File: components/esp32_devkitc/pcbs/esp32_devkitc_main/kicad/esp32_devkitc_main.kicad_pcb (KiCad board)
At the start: 2 copper layers, 65 x 56 mm, 28 parts, among them J1 Conn_02x05_Odd_Even, J2 Conn_02x04_Odd_Even, J3 Conn_01x03_Male, J4 Conn_01x02, P1 Conn_02x20_Odd_Even, U1 ESP32-DEVKITC-32D

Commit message: small update
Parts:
- J4: moved to B.Cu
- P1: footprint Connector_PinSocket_2.54mm:PinSocket_2x20_P2.54mm_Vertical -> Connector_PinHeader_2.54mm:PinHeader_2x20_P2.54mm_Vertical; moved to F.Cu
- turned J4 to 90 degrees
- turned P1 to 90 degrees
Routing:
- net /SENS_5V_ANA: track 100.2 -> 100.9 mm

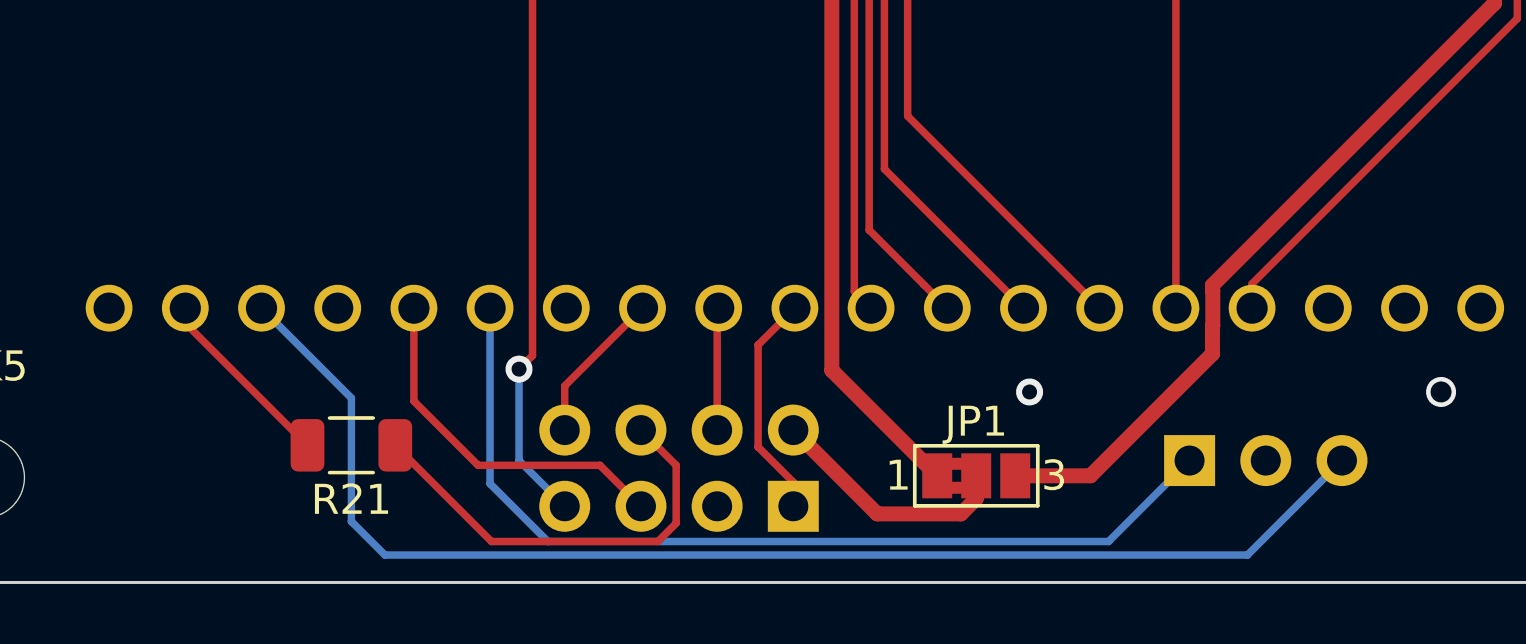
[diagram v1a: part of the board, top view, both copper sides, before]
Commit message: moves R21 below devkit
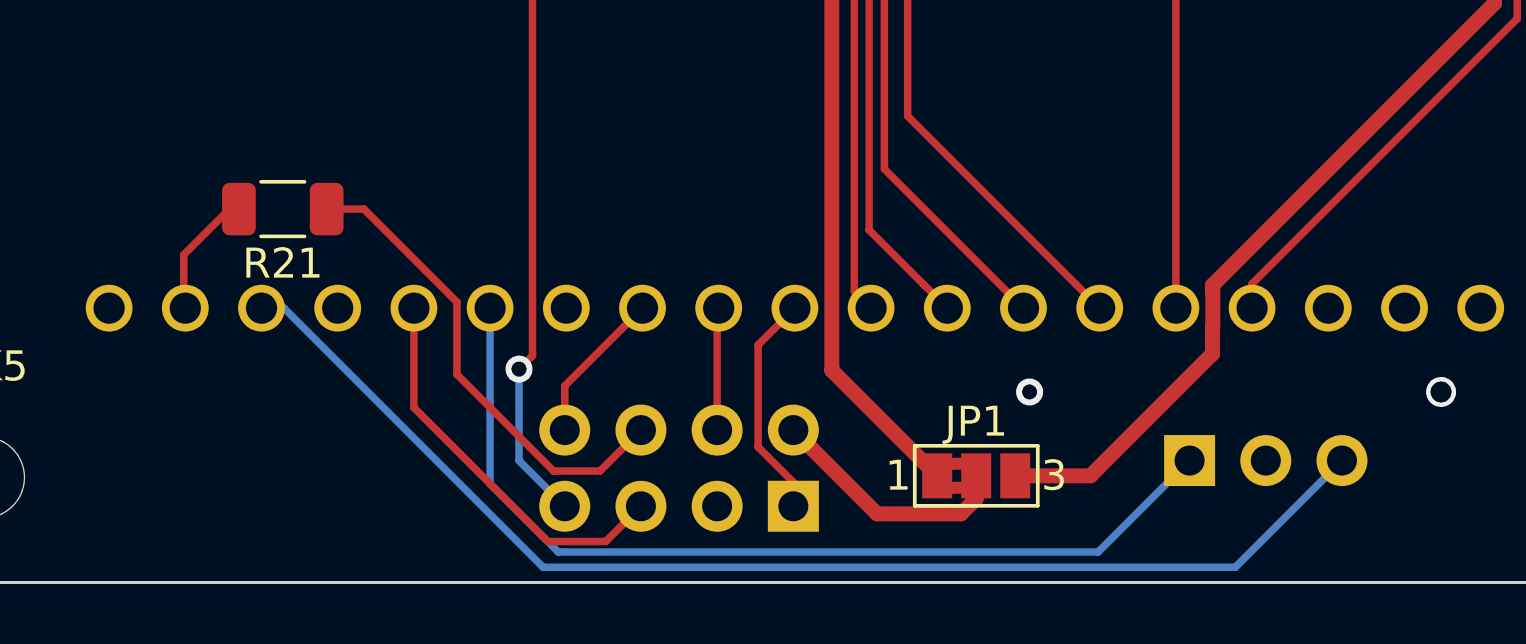
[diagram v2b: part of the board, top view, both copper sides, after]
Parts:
- moved R21 8.20 mm to (213.5, 137.6)
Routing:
- net /PROC_SCL: track 43.1 -> 41.1 mm
- net Net-(R21-Pad2): track 6.26 -> 4.27 mm
- net /DISP_MOSI: track 14.5 -> 16.1 mm
- net /DISP_CS_TOUCH: track 12.1 -> 13.2 mm
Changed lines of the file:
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@@
     (thickness 1.6)
     (drawings 21)
-    (tracks 261)
+    (tracks 263)
     (zones 0)
     (modules 28)
@@
     (pad_to_mask_clearance 0)
     (aux_axis_origin 200 150)
-    (grid_origin 200 150)
     (visible_elements 7FFFFFFF)
     (pcbplotparams
@@
   )
   (module Resistor_SMD:R_1206_3216Metric (layer F.Cu)
-    (at 215.748 145.428 180)
+    (at 213.462 137.554 180)
     (descr "Resistor SMD 1206 (3216 Metric), square (rectangular) end terminal, IPC_7351 nominal, (Body size source: IPC-SM-782 page 72, https://www.pcb-3d.com/wordpress/wp-content/uploads/ipc-sm-782a_amendment_1_and_2.pdf), generated with kicad-footprint-generator")
     (tags resistor)
@@
   (segment (start 246.7975 107.328) (end 244.45 107.328) (width 0.25) (layer F.Cu) (net 41))
   (via (at 244.45 107.328) (size 0.9) (drill 0.5) (layers F.Cu B.Cu) (net 41))
-  (segment (start 216.865011 149.085011) (end 245.618989 149.085011) (width 0.25) (layer B.Cu) (net 42))
-  (segment (start 215.748 147.968) (end 216.865011 149.085011) (width 0.25) (layer B.Cu) (net 42))
-  (segment (start 215.748 143.852) (end 215.748 147.968) (width 0.25) (layer B.Cu) (net 42))
-  (segment (start 245.618989 149.085011) (end 248.768 145.936) (width 0.25) (layer B.Cu) (net 42))
-  (segment (start 212.752 140.856) (end 215.748 143.852) (width 0.25) (layer B.Cu) (net 42))
-  (segment (start 220.372 146.711002) (end 222.295999 148.635001) (width 0.25) (layer B.Cu) (net 43))
-  (segment (start 240.988999 148.635001) (end 243.688 145.936) (width 0.25) (layer B.Cu) (net 43))
-  (segment (start 222.295999 148.635001) (end 240.988999 148.635001) (width 0.25) (layer B.Cu) (net 43))
+  (segment (start 245.212 149.492) (end 248.768 145.936) (width 0.25) (layer B.Cu) (net 42))
+  (segment (start 222.136 149.492) (end 245.212 149.492) (width 0.25) (layer B.Cu) (net 42))
+  (segment (start 213.5 140.856) (end 222.136 149.492) (width 0.25) (layer B.Cu) (net 42))
+  (segment (start 212.752 140.856) (end 213.5 140.856) (width 0.25) (layer B.Cu) (net 42))
+  (segment (start 240.64 148.984) (end 243.688 145.936) (width 0.25) (layer B.Cu) (net 43))
+  (segment (start 222.644998 148.984) (end 240.64 148.984) (width 0.25) (layer B.Cu) (net 43))
+  (segment (start 220.372 146.711002) (end 222.644998 148.984) (width 0.25) (layer B.Cu) (net 43))
   (segment (start 220.372 140.856) (end 220.372 146.711002) (width 0.25) (layer B.Cu) (net 43))
   (segment (start 259.784999 108.184999) (end 260.96 109.36) (width 0.25) (layer F.Cu) (net 44))
@@
   (segment (start 221.785999 142.438001) (end 221.785999 119.324001) (width 0.25) (layer F.Cu) (net 48))
   (segment (start 221.785999 119.324001) (end 221.844 119.266) (width 0.25) (layer F.Cu) (net 48))
-  (segment (start 226.575001 148.024001) (end 226.575001 146.095001) (width 0.25) (layer F.Cu) (net 49))
-  (segment (start 226.575001 146.095001) (end 225.4 144.92) (width 0.25) (layer F.Cu) (net 49))
-  (segment (start 225.964001 148.635001) (end 226.575001 148.024001) (width 0.25) (layer F.Cu) (net 49))
-  (segment (start 220.417501 148.635001) (end 225.964001 148.635001) (width 0.25) (layer F.Cu) (net 49))
-  (segment (start 217.2105 145.428) (end 220.417501 148.635001) (width 0.25) (layer F.Cu) (net 49))
+  (segment (start 224.035001 146.284999) (end 225.4 144.92) (width 0.25) (layer F.Cu) (net 49))
+  (segment (start 222.485997 146.284999) (end 224.035001 146.284999) (width 0.25) (layer F.Cu) (net 49))
+  (segment (start 219.266999 143.066001) (end 222.485997 146.284999) (width 0.25) (layer F.Cu) (net 49))
+  (segment (start 219.266999 140.655597) (end 219.266999 143.066001) (width 0.25) (layer F.Cu) (net 49))
+  (segment (start 216.165402 137.554) (end 219.266999 140.655597) (width 0.25) (layer F.Cu) (net 49))
+  (segment (start 214.9245 137.554) (end 216.165402 137.554) (width 0.25) (layer F.Cu) (net 49))
   (segment (start 236.576 147.204002) (end 236.576 146.444) (width 0.5) (layer F.Cu) (net 50))
   (segment (start 236.066002 147.714) (end 236.576 147.204002) (width 0.5) (layer F.Cu) (net 50))
@@
   (segment (start 228.448 106.2505) (end 226.557001 108.141499) (width 0.25) (layer F.Cu) (net 54))
   (segment (start 226.557001 115.656403) (end 233.006998 122.1064) (width 0.25) (layer F.Cu) (net 54))
-  (segment (start 210.212 141.3545) (end 210.212 140.856) (width 0.25) (layer F.Cu) (net 55))
-  (segment (start 214.2855 145.428) (end 210.212 141.3545) (width 0.25) (layer F.Cu) (net 55))
+  (segment (start 210.16 140.804) (end 210.212 140.856) (width 0.25) (layer F.Cu) (net 55))
+  (segment (start 210.16 139.078) (end 210.16 140.804) (width 0.25) (layer F.Cu) (net 55))
+  (segment (start 211.684 137.554) (end 210.16 139.078) (width 0.25) (layer F.Cu) (net 55))
+  (segment (start 211.9995 137.554) (end 211.684 137.554) (width 0.25) (layer F.Cu) (net 55))
   (segment (start 227.992 115.456) (end 236.322 107.126) (width 0.25) (layer F.Cu) (net 56))
   (segment (start 236.322 107.126) (end 236.322 106.82) (width 0.25) (layer F.Cu) (net 56))
   (segment (start 236.322 106.82) (end 236.322 106.566) (width 0.25) (layer F.Cu) (net 56))
-  (segment (start 217.832 140.856) (end 217.832 143.956) (width 0.25) (layer F.Cu) (net 57))
-  (segment (start 217.832 143.956) (end 219.971001 146.095001) (width 0.25) (layer F.Cu) (net 57))
-  (segment (start 219.971001 146.095001) (end 224.035001 146.095001) (width 0.25) (layer F.Cu) (net 57))
-  (segment (start 224.035001 146.095001) (end 225.4 147.46) (width 0.25) (layer F.Cu) (net 57))
+  (segment (start 224.224999 148.635001) (end 225.4 147.46) (width 0.25) (layer F.Cu) (net 57))
+  (segment (start 222.295999 148.635001) (end 224.224999 148.635001) (width 0.25) (layer F.Cu) (net 57))
+  (segment (start 217.832 144.171002) (end 222.295999 148.635001) (width 0.25) (layer F.Cu) (net 57))
+  (segment (start 217.832 140.856) (end 217.832 144.171002) (width 0.25) (layer F.Cu) (net 57))
   (segment (start 229.304999 142.083001) (end 230.532 140.856) (width 0.25) (layer F.Cu) (net 58) (status 20))
   (segment (start 229.304999 145.484001) (end 229.304999 142.083001) (width 0.25) (layer F.Cu) (net 58))

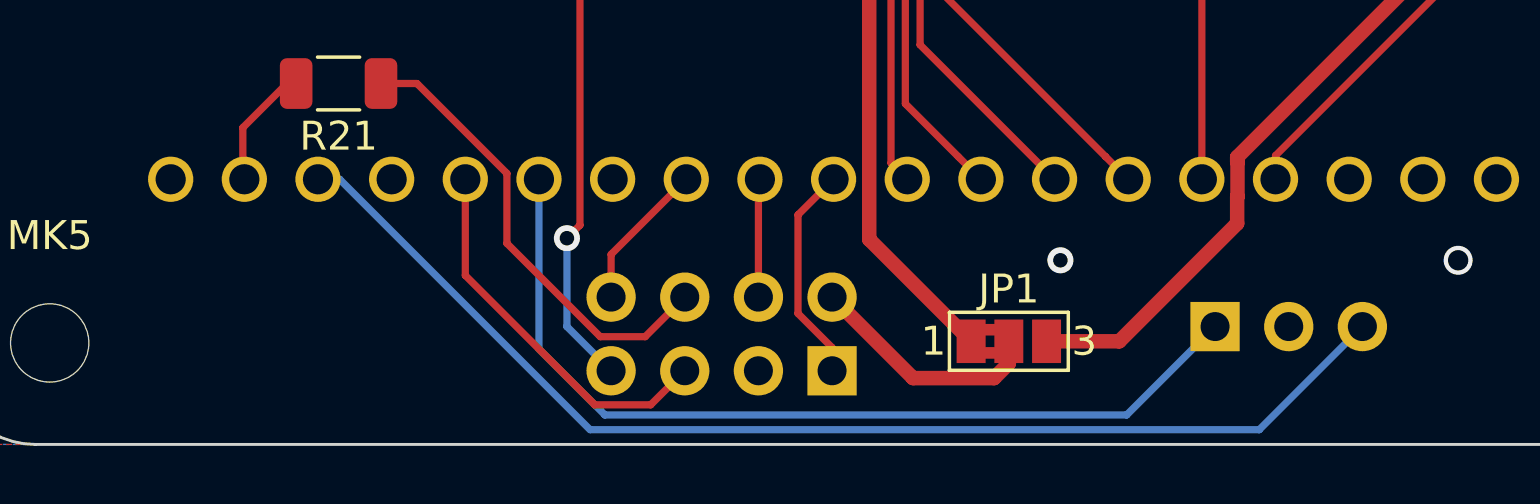
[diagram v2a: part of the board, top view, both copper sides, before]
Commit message: removes filling
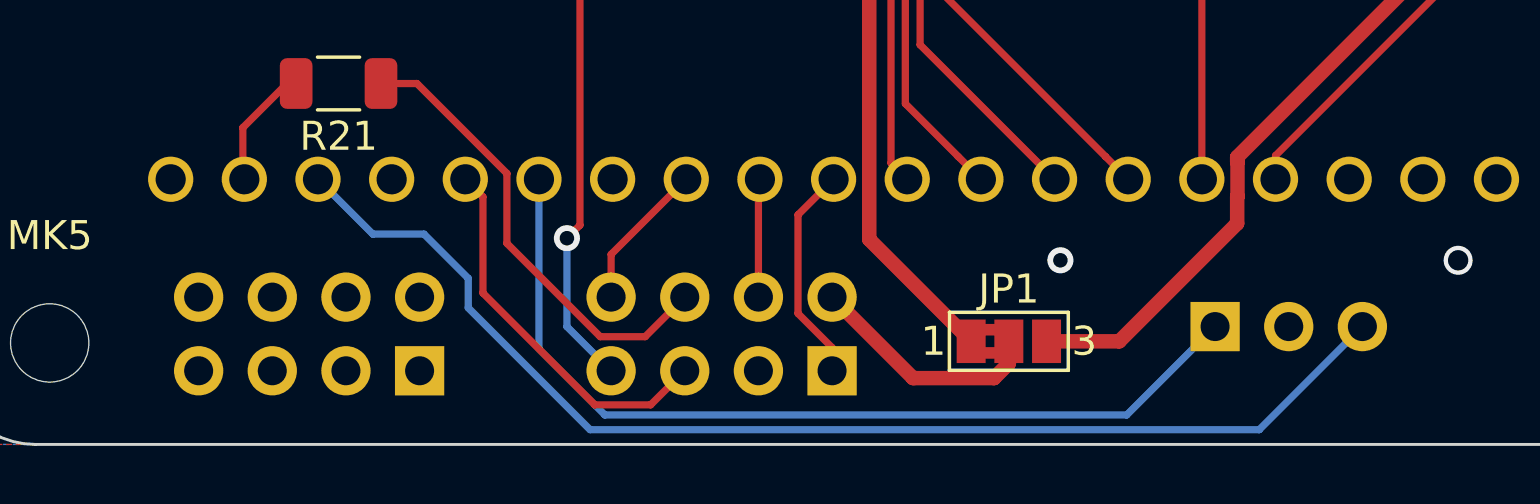
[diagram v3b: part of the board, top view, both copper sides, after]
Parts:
- added J2: Conn_02x04_Odd_Even, Connector_PinHeader_2.54mm:PinHeader_2x04_P2.54mm_Vertical, B.Cu at (216.3, 147.5)
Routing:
- net /PROC_SCL: track 41.1 -> 41.7 mm
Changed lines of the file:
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@@
     (thickness 1.6)
     (drawings 21)
-    (tracks 263)
+    (tracks 267)
     (zones 0)
-    (modules 28)
+    (modules 29)
     (nets 68)
   )
@@
     (diff_pair_gap 0.25)
     (add_net GND)
+  )
+  (module Connector_PinHeader_2.54mm:PinHeader_2x04_P2.54mm_Vertical (layer B.Cu)
+    (at 216.256 147.46 90)
+    (descr "Through hole straight pin header, 2x04, 2.54mm pitch, double rows")
+    (tags "Through hole pin header THT 2x04 2.54mm double row")
+    (fp_text reference J2 (at 1.27 2.33 90) (layer B.SilkS)
+      (effects (font (size 1 1) (thickness 0.15)) (justify mirror))
+    )
+    (fp_text value Conn_02x04_Odd_Even (at 1.27 -9.95 90) (layer B.Fab)
+      (effects (font (size 1 1) (thickness 0.15)) (justify mirror))
+    )
+    (fp_line (start 0 1.27) (end 3.81 1.27) (layer B.Fab) (width 0.1))
+    (fp_line (start 3.81 1.27) (end 3.81 -8.89) (layer B.Fab) (width 0.1))
+    (fp_line (start 3.81 -8.89) (end -1.27 -8.89) (layer B.Fab) (width 0.1))
+    (fp_line (start -1.27 -8.89) (end -1.27 0) (layer B.Fab) (width 0.1))
+    (fp_line (start -1.27 0) (end 0 1.27) (layer B.Fab) (width 0.1))
+    (fp_line (start -1.33 -8.95) (end 3.87 -8.95) (layer B.SilkS) (width 0.12))
+    (fp_line (start -1.33 -1.27) (end -1.33 -8.95) (layer B.SilkS) (width 0.12))
+    (fp_line (start 3.87 1.33) (end 3.87 -8.95) (layer B.SilkS) (width 0.12))
+    (fp_line (start -1.33 -1.27) (end 1.27 -1.27) (layer B.SilkS) (width 0.12))
+    (fp_line (start 1.27 -1.27) (end 1.27 1.33) (layer B.SilkS) (width 0.12))
+    (fp_line (start 1.27 1.33) (end 3.87 1.33) (layer B.SilkS) (width 0.12))
+    (fp_line (start -1.33 0) (end -1.33 1.33) (layer B.SilkS) (width 0.12))
+    (fp_line (start -1.33 1.33) (end 0 1.33) (layer B.SilkS) (width 0.12))
+    (fp_line (start -1.8 1.8) (end -1.8 -9.4) (layer B.CrtYd) (width 0.05))
+    (fp_line (start -1.8 -9.4) (end 4.35 -9.4) (layer B.CrtYd) (width 0.05))
+    (fp_line (start 4.35 -9.4) (end 4.35 1.8) (layer B.CrtYd) (width 0.05))
+    (fp_line (start 4.35 1.8) (end -1.8 1.8) (layer B.CrtYd) (width 0.05))
+    (fp_text user %R (at 1.27 -3.81 180) (layer B.Fab)
+      (effects (font (size 1 1) (thickness 0.15)) (justify mirror))
+    )
+    (pad 1 thru_hole rect (at 0 0 90) (size 1.7 1.7) (drill 1) (layers *.Cu *.Mask))
+    (pad 2 thru_hole oval (at 2.54 0 90) (size 1.7 1.7) (drill 1) (layers *.Cu *.Mask))
+    (pad 3 thru_hole oval (at 0 -2.54 90) (size 1.7 1.7) (drill 1) (layers *.Cu *.Mask))
+    (pad 4 thru_hole oval (at 2.54 -2.54 90) (size 1.7 1.7) (drill 1) (layers *.Cu *.Mask))
+    (pad 5 thru_hole oval (at 0 -5.08 90) (size 1.7 1.7) (drill 1) (layers *.Cu *.Mask))
+    (pad 6 thru_hole oval (at 2.54 -5.08 90) (size 1.7 1.7) (drill 1) (layers *.Cu *.Mask))
+    (pad 7 thru_hole oval (at 0 -7.62 90) (size 1.7 1.7) (drill 1) (layers *.Cu *.Mask))
+    (pad 8 thru_hole oval (at 2.54 -7.62 90) (size 1.7 1.7) (drill 1) (layers *.Cu *.Mask))
+    (model ${KISYS3DMOD}/Connector_PinHeader_2.54mm.3dshapes/PinHeader_2x04_P2.54mm_Vertical.wrl
+      (at (xyz 0 0 0))
+      (scale (xyz 1 1 1))
+      (rotate (xyz 0 0 0))
+    )
   )
   (module Connector_PinHeader_2.54mm:PinHeader_2x04_P2.54mm_Vertical (layer B.Cu)
@@
   (segment (start 246.7975 107.328) (end 244.45 107.328) (width 0.25) (layer F.Cu) (net 41))
   (via (at 244.45 107.328) (size 0.9) (drill 0.5) (layers F.Cu B.Cu) (net 41))
-  (segment (start 245.212 149.492) (end 248.768 145.936) (width 0.25) (layer B.Cu) (net 42))
-  (segment (start 222.136 149.492) (end 245.212 149.492) (width 0.25) (layer B.Cu) (net 42))
-  (segment (start 213.5 140.856) (end 222.136 149.492) (width 0.25) (layer B.Cu) (net 42))
-  (segment (start 212.752 140.856) (end 213.5 140.856) (width 0.25) (layer B.Cu) (net 42))
+  (segment (start 214.644 142.748) (end 212.752 140.856) (width 0.25) (layer B.Cu) (net 42))
+  (segment (start 216.408 142.748) (end 214.644 142.748) (width 0.25) (layer B.Cu) (net 42))
+  (segment (start 222.136 149.492) (end 217.932 145.288) (width 0.25) (layer B.Cu) (net 42))
+  (segment (start 217.932 144.272) (end 216.408 142.748) (width 0.25) (layer B.Cu) (net 42))
+  (segment (start 217.932 145.288) (end 217.932 144.272) (width 0.25) (layer B.Cu) (net 42))
+  (segment (start 245.212 149.492) (end 222.136 149.492) (width 0.25) (layer B.Cu) (net 42))
+  (segment (start 248.768 145.936) (end 245.212 149.492) (width 0.25) (layer B.Cu) (net 42))
   (segment (start 240.64 148.984) (end 243.688 145.936) (width 0.25) (layer B.Cu) (net 43))
   (segment (start 222.644998 148.984) (end 240.64 148.984) (width 0.25) (layer B.Cu) (net 43))
@@
   (segment (start 224.224999 148.635001) (end 225.4 147.46) (width 0.25) (layer F.Cu) (net 57))
   (segment (start 222.295999 148.635001) (end 224.224999 148.635001) (width 0.25) (layer F.Cu) (net 57))
-  (segment (start 217.832 144.171002) (end 222.295999 148.635001) (width 0.25) (layer F.Cu) (net 57))
-  (segment (start 217.832 140.856) (end 217.832 144.171002) (width 0.25) (layer F.Cu) (net 57))
+  (segment (start 218.44 144.779002) (end 222.295999 148.635001) (width 0.25) (layer F.Cu) (net 57))
+  (segment (start 218.44 141.464) (end 218.44 144.779002) (width 0.25) (layer F.Cu) (net 57))
+  (segment (start 217.832 140.856) (end 218.44 141.464) (width 0.25) (layer F.Cu) (net 57))
   (segment (start 229.304999 142.083001) (end 230.532 140.856) (width 0.25) (layer F.Cu) (net 58) (status 20))
   (segment (start 229.304999 145.484001) (end 229.304999 142.083001) (width 0.25) (layer F.Cu) (net 58))
@@
     (connect_pads (clearance 0.3))
     (min_thickness 0.254)
-    (fill yes (arc_segments 32) (thermal_gap 0.508) (thermal_bridge_width 0.508))
+    (fill (arc_segments 32) (thermal_gap 0.508) (thermal_bridge_width 0.508))
     (polygon
       (pts
@@
     (connect_pads (clearance 0.508))
     (min_thickness 0.254)
-    (fill yes (arc_segments 32) (thermal_gap 0.508) (thermal_bridge_width 0.508))
+    (fill (arc_segments 32) (thermal_gap 0.508) (thermal_bridge_width 0.508))
     (polygon
       (pts
